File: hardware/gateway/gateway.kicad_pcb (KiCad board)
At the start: 2 copper layers, 65 x 32 mm, 29 parts, among them J1 FTDI, J2 Conn_Coaxial, J3 Raspberry_Pi_2_3, U1 RFM69HW, U2 DS1307Z+, U3 AP130-xxY, Y1 32768

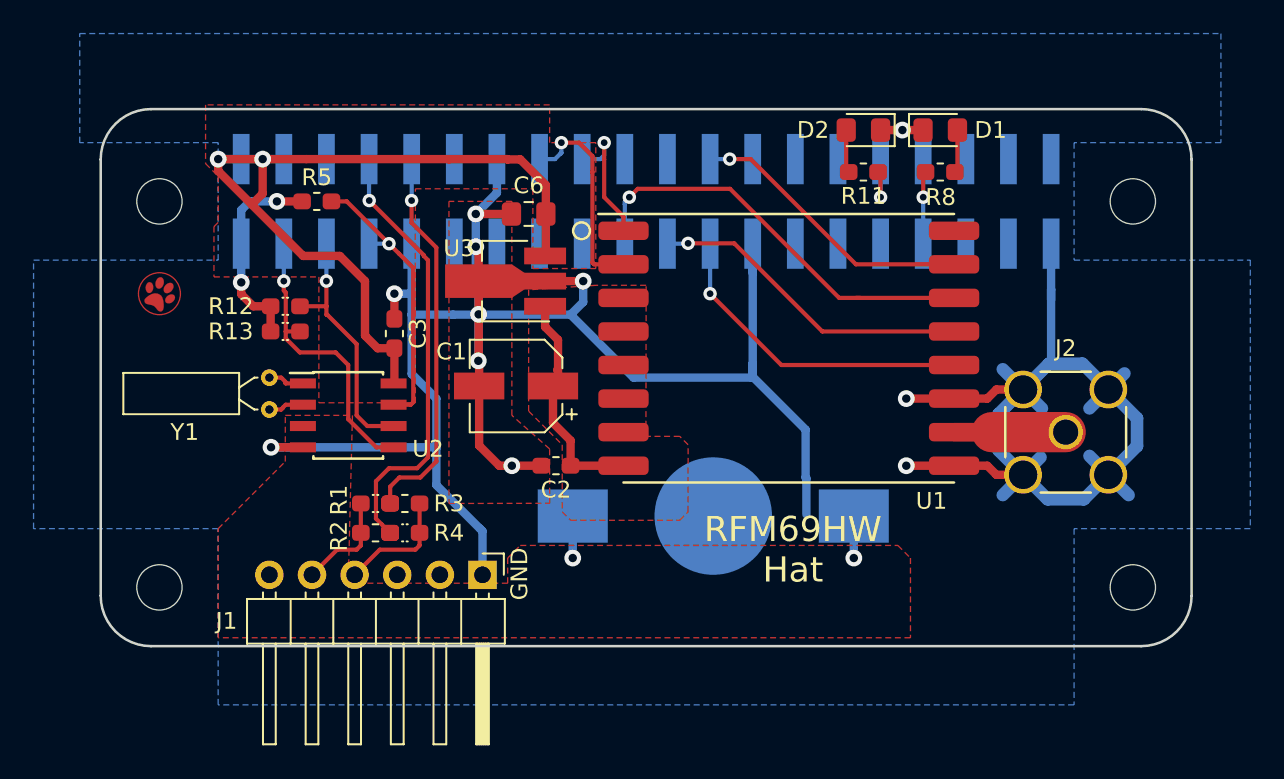
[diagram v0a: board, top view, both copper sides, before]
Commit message: Added extra input cap and CS pullup to gateway
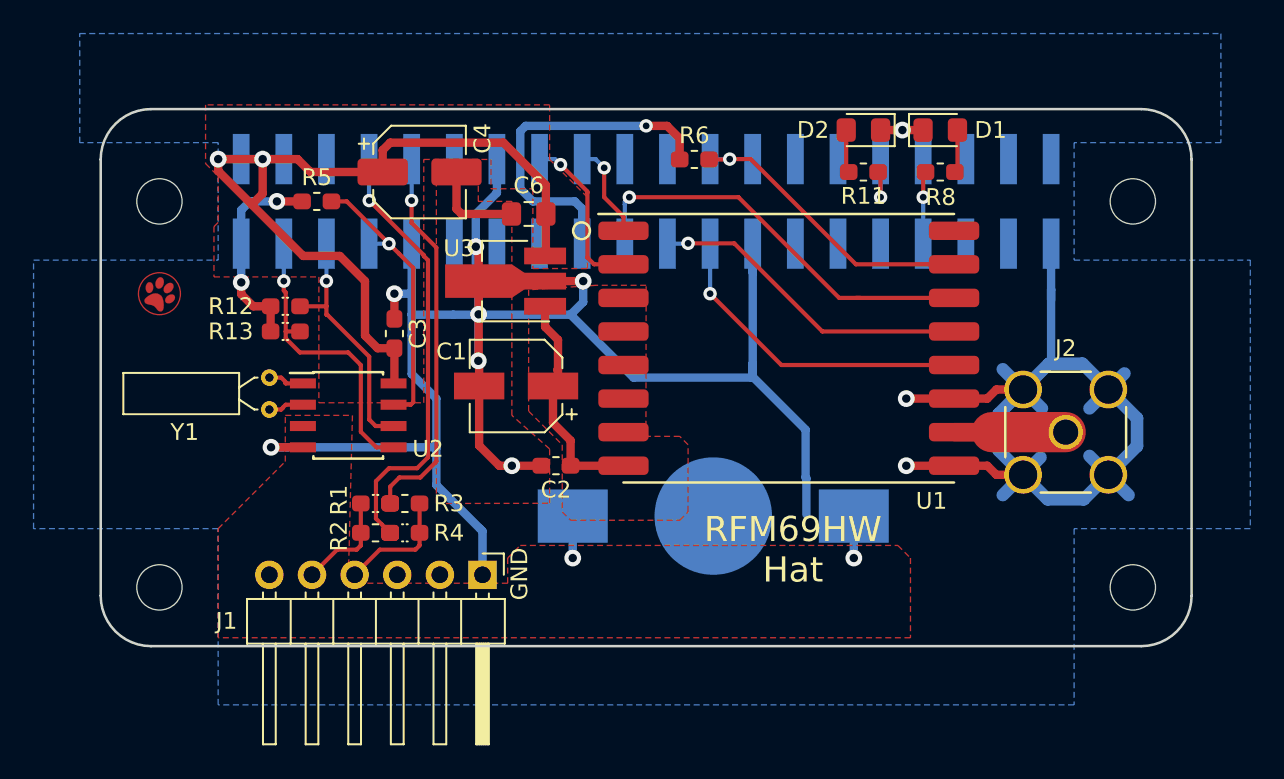
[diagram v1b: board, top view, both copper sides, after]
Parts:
- added C4: 22u, Capacitor_SMD:CP_Elec_5x5.3, F.Cu at (115.5, 48.2)
- added R6: 10k, Resistor_SMD:R_0603_1608Metric_Pad1.05x0.95mm_HandSolder, F.Cu at (131.9, 47.5)
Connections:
- J3 pad 17: Net-(J3-Pad17) -> /3V3_PI_17
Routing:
- net /3V3_PI_17: track 0.00 -> 20.9 mm, vias 0 -> 1
- net GND: track 182.6 -> 186.0 mm, vias 11 -> 10
- net /RFM_INT: track 12.5 -> 9.91 mm
- net +5V_PI: track 50.9 -> 53.1 mm
- net /RFM_RESET: track 7.88 -> 5.76 mm
- net /CS: track 17.1 -> 18.4 mm

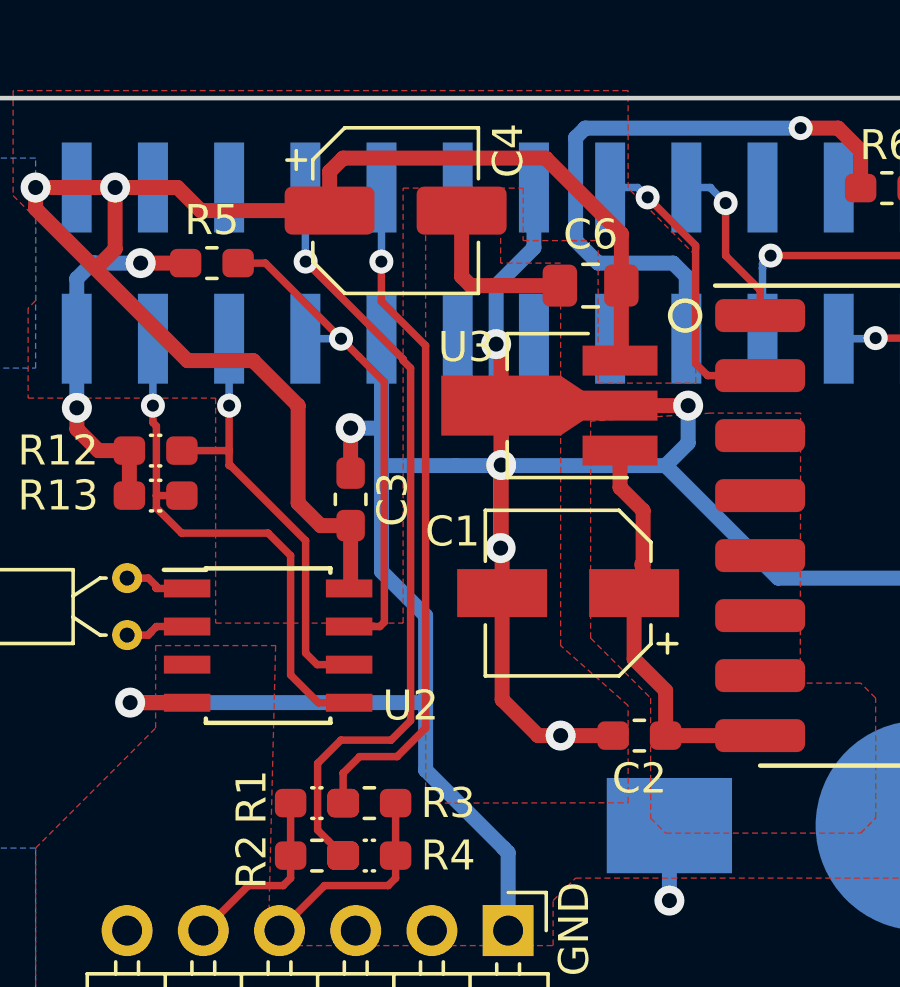
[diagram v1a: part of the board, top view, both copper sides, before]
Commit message: Improved GND
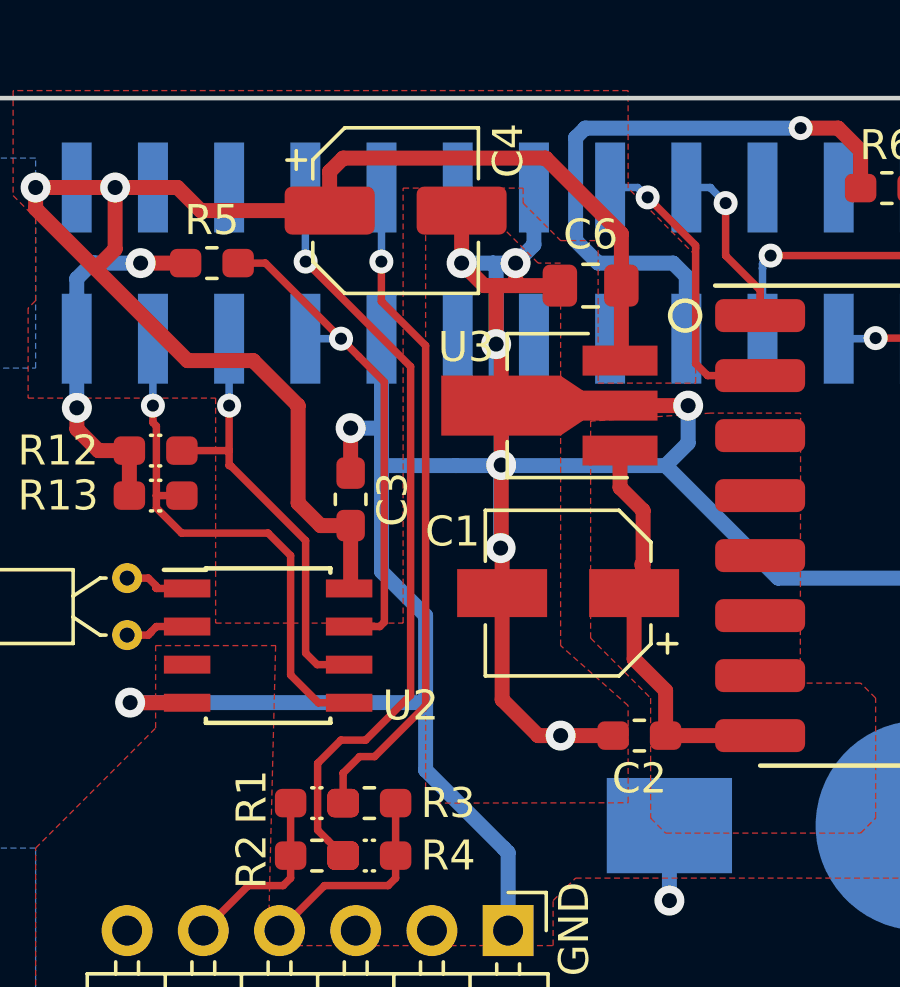
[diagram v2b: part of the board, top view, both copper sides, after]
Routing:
- net GND: track 186.0 -> 190.0 mm, vias 10 -> 12

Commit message: Small udjustments to gateway PCB
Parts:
- moved G*** 0.50 mm to (100.0, 56.0)
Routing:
- net /VBAT: track 5.00 -> 63.0 mm
- net GND: track 190.0 -> 186.8 mm
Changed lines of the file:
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@@
     (thickness 1.6)
     (drawings 20)
-    (tracks 310)
+    (tracks 317)
     (zones 0)
     (modules 31)
@@
   )
   (module humidity:paw-cu-circ (layer F.Cu)
-    (at 100 55.5 330)
+    (at 100 56 330)
     (fp_text reference G*** (at 0 0 330) (layer F.SilkS) hide
       (effects (font (size 1.524 1.524) (thickness 0.3)))
@@
   (segment (start 119.25 72.25) (end 119.25 69.65) (width 0.5) (layer B.Cu) (net 9))
   (segment (start 116.5 66.9) (end 119.1 69.5) (width 0.5) (layer B.Cu) (net 9))
-  (segment (start 135.35 60.45) (end 135.35 59.65) (width 0.5) (layer B.Cu) (net 9))
-  (segment (start 135.35 52.52) (end 135.35 59.65) (width 0.5) (layer B.Cu) (net 9))
-  (segment (start 135.35 59.65) (end 135.35 60.25) (width 0.5) (layer B.Cu) (net 9))
-  (segment (start 138.5 66.45) (end 138.5 63.6) (width 0.5) (layer B.Cu) (net 9))
-  (segment (start 138.55 66.5) (end 138.5 66.45) (width 0.5) (layer B.Cu) (net 9))
-  (segment (start 138.55 68.65) (end 138.55 66.5) (width 0.5) (layer B.Cu) (net 9))
-  (segment (start 138.5 63.6) (end 135.35 60.45) (width 0.5) (layer B.Cu) (net 9))
   (segment (start 153.13 52.52) (end 153.13 55.25) (width 0.5) (layer B.Cu) (net 9))
   (segment (start 153.13 55.25) (end 153.13 55.88) (width 0.5) (layer B.Cu) (net 9))
@@
   (segment (start 124.5 56.75) (end 125.25 56) (width 0.5) (layer B.Cu) (net 9))
   (segment (start 124.5 56.75) (end 128.25 60.5) (width 0.5) (layer B.Cu) (net 9))
-  (segment (start 135.3 60.5) (end 135.35 60.45) (width 0.5) (layer B.Cu) (net 9))
-  (segment (start 128.25 60.5) (end 135.3 60.5) (width 0.5) (layer B.Cu) (net 9))
   (segment (start 156.54 61.21) (end 158.25 62.92) (width 0.75) (layer B.Cu) (net 9))
   (segment (start 158.25 64.58) (end 156.54 66.29) (width 0.75) (layer B.Cu) (net 9))
@@
   (segment (start 118.85 50.75) (end 119.5 50.75) (width 0.5) (layer F.Cu) (net 9))
   (segment (start 119.5 50.75) (end 120.975 50.75) (width 0.5) (layer F.Cu) (net 9))
+  (segment (start 128.25 60.5) (end 133 60.5) (width 0.5) (layer B.Cu) (net 9))
+  (segment (start 133 68.75) (end 133 60.5) (width 0.5) (layer B.Cu) (net 9))
+  (segment (start 133 60.35) (end 135.35 58) (width 0.5) (layer B.Cu) (net 9))
+  (segment (start 133 60.5) (end 133 60.35) (width 0.5) (layer B.Cu) (net 9))
+  (segment (start 135.35 52.52) (end 135.35 58) (width 0.5) (layer B.Cu) (net 9))
   (segment (start 115.5 69.75) (end 115.5 68) (width 0.25) (layer F.Cu) (net 10))
   (segment (start 115.5 70.5) (end 115.5 69.75) (width 0.25) (layer F.Cu) (net 10))
@@
   (segment (start 141.374 71.249) (end 141.375 71.25) (width 0.5) (layer B.Cu) (net 41))
   (segment (start 141.374 68.75) (end 141.374 71.249) (width 0.5) (layer B.Cu) (net 41))
+  (segment (start 108.55 63.385) (end 109.885 63.385) (width 0.5) (layer F.Cu) (net 41))
+  (segment (start 109.885 63.385) (end 110.25 63.75) (width 0.5) (layer F.Cu) (net 41))
+  (segment (start 110.25 63.75) (end 110.25 65.25) (width 0.5) (layer F.Cu) (net 41))
+  (segment (start 110.25 65.25) (end 104.5 71) (width 0.5) (layer F.Cu) (net 41))
+  (segment (start 104.5 71) (end 104.5 73.75) (width 0.5) (layer F.Cu) (net 41))
+  (segment (start 104.5 73.75) (end 105.5 74.75) (width 0.5) (layer F.Cu) (net 41))
+  (segment (start 141.375 73.875) (end 141.375 71.25) (width 0.5) (layer F.Cu) (net 41))
+  (segment (start 140.5 74.75) (end 141.375 73.875) (width 0.5) (layer F.Cu) (net 41))
+  (segment (start 105.5 74.75) (end 124.626 74.75) (width 0.5) (layer F.Cu) (net 41))
+  (segment (start 124.626 71.25) (end 124.626 74.75) (width 0.5) (layer F.Cu) (net 41))
+  (segment (start 124.626 74.75) (end 140.5 74.75) (width 0.5) (layer F.Cu) (net 41))
   (segment (start 123.75 60.25) (end 123.75 60.5) (width 0.5) (layer F.Cu) (net 42))
   (segment (start 123.75 60) (end 123.75 60.5) (width 0.5) (layer F.Cu) (net 42))
